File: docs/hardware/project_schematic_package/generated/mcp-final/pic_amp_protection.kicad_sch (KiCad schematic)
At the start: 3 parts, among them U1 MCU, U2 74HC4514, U3 ULN2803A

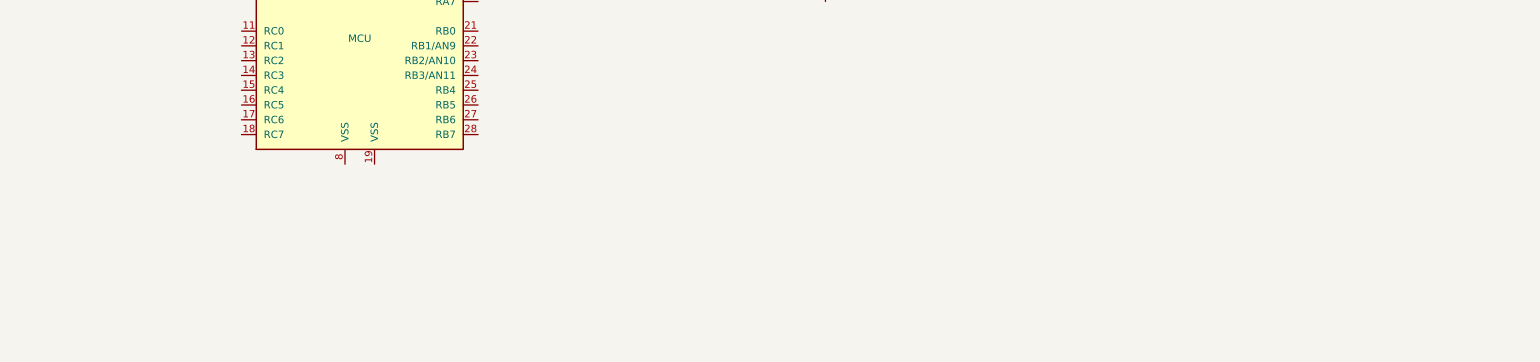
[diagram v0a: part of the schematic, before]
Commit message: Checkpoint MCP schematic layout and developer setup
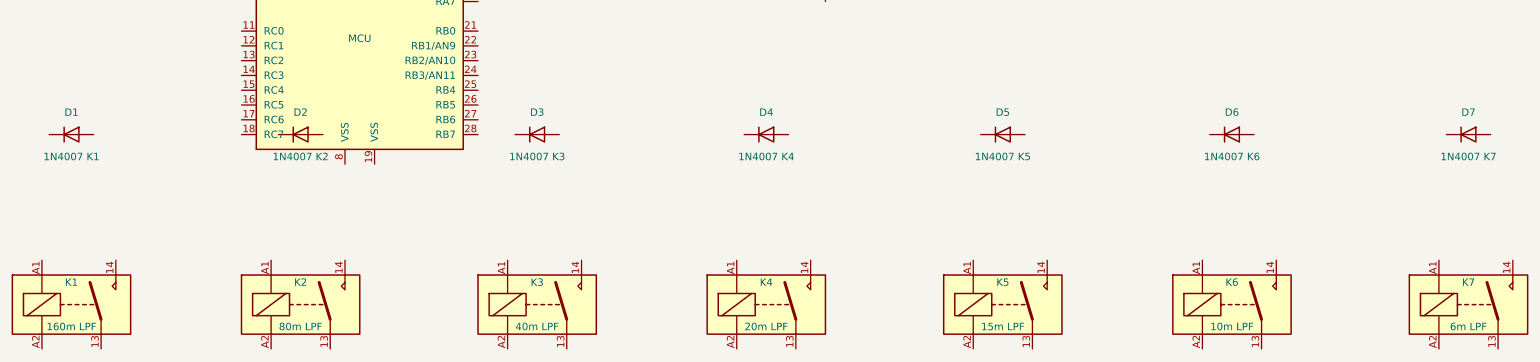
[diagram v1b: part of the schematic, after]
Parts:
- added D1: 1N4007 K1, symbol Device:D
- added D2: 1N4007 K2, symbol Device:D
- added D3: 1N4007 K3, symbol Device:D
- added D4: 1N4007 K4, symbol Device:D
- added D5: 1N4007 K5, symbol Device:D
- added D6: 1N4007 K6, symbol Device:D
- added D7: 1N4007 K7, symbol Device:D
- added K1: 160m LPF, symbol Relay:Relay_SPST-NO
- added K2: 80m LPF, symbol Relay:Relay_SPST-NO
- added K3: 40m LPF, symbol Relay:Relay_SPST-NO
- added K4: 20m LPF, symbol Relay:Relay_SPST-NO
- added K5: 15m LPF, symbol Relay:Relay_SPST-NO
- added K6: 10m LPF, symbol Relay:Relay_SPST-NO
- added K7: 6m LPF, symbol Relay:Relay_SPST-NO

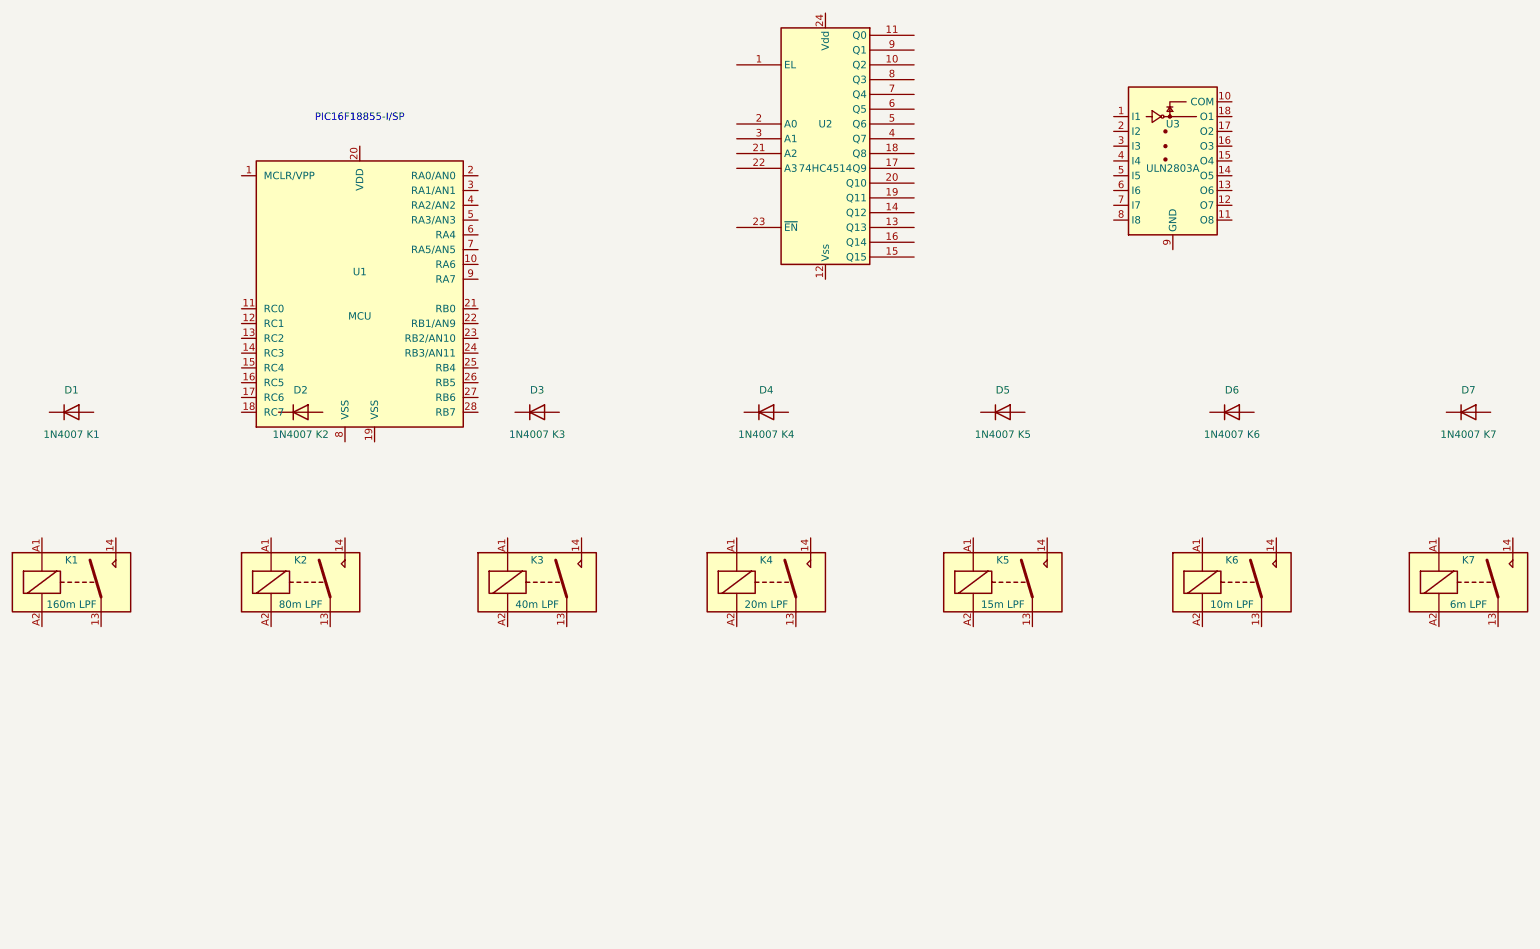
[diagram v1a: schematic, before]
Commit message: Add schematic external interface headers
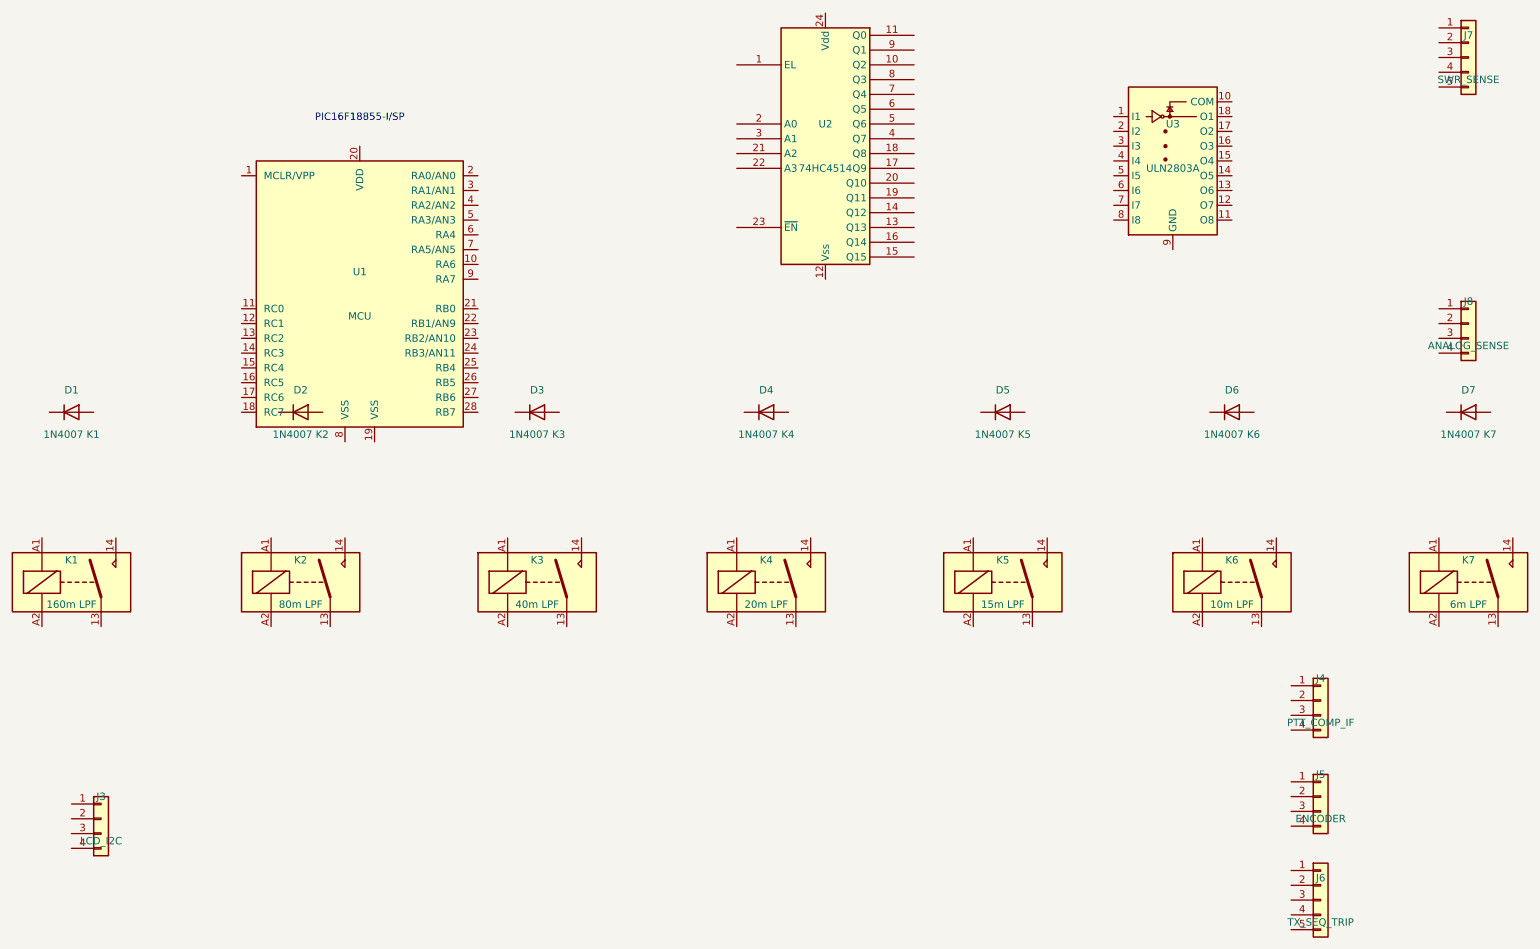
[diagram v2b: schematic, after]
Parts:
- added J3: LCD_I2C, symbol Connector_Generic:Conn_01x04
- added J4: PTT_COMP_IF, symbol Connector_Generic:Conn_01x04
- added J5: ENCODER, symbol Connector_Generic:Conn_01x04
- added J6: TX_SEQ_TRIP, symbol Connector_Generic:Conn_01x05
- added J7: SWR_SENSE, symbol Connector_Generic:Conn_01x05
- added J8: ANALOG_SENSE, symbol Connector_Generic:Conn_01x04

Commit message: Assign PIC16F18855 narrow SPDIP footprint
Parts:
- U1: footprint (none) -> Package_DIP:DIP-28_W7.62mm
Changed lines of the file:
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@@
 		)
 	)
-	(property "Footprint" ""
+	(property "Footprint" "Package_DIP:DIP-28_W7.62mm"
 		(at 80.01 95.25 0)
 		(effects
@@
 			(unit 1)
 			(value "MCU")
-			(footprint "")
+			(footprint "Package_DIP:DIP-28_W7.62mm")
 		)
 		(path "/5f892659-1480-447d-b5a7-bee1c920df64/b79ec903-e143-4f75-9899-3a3ede06d9cd"

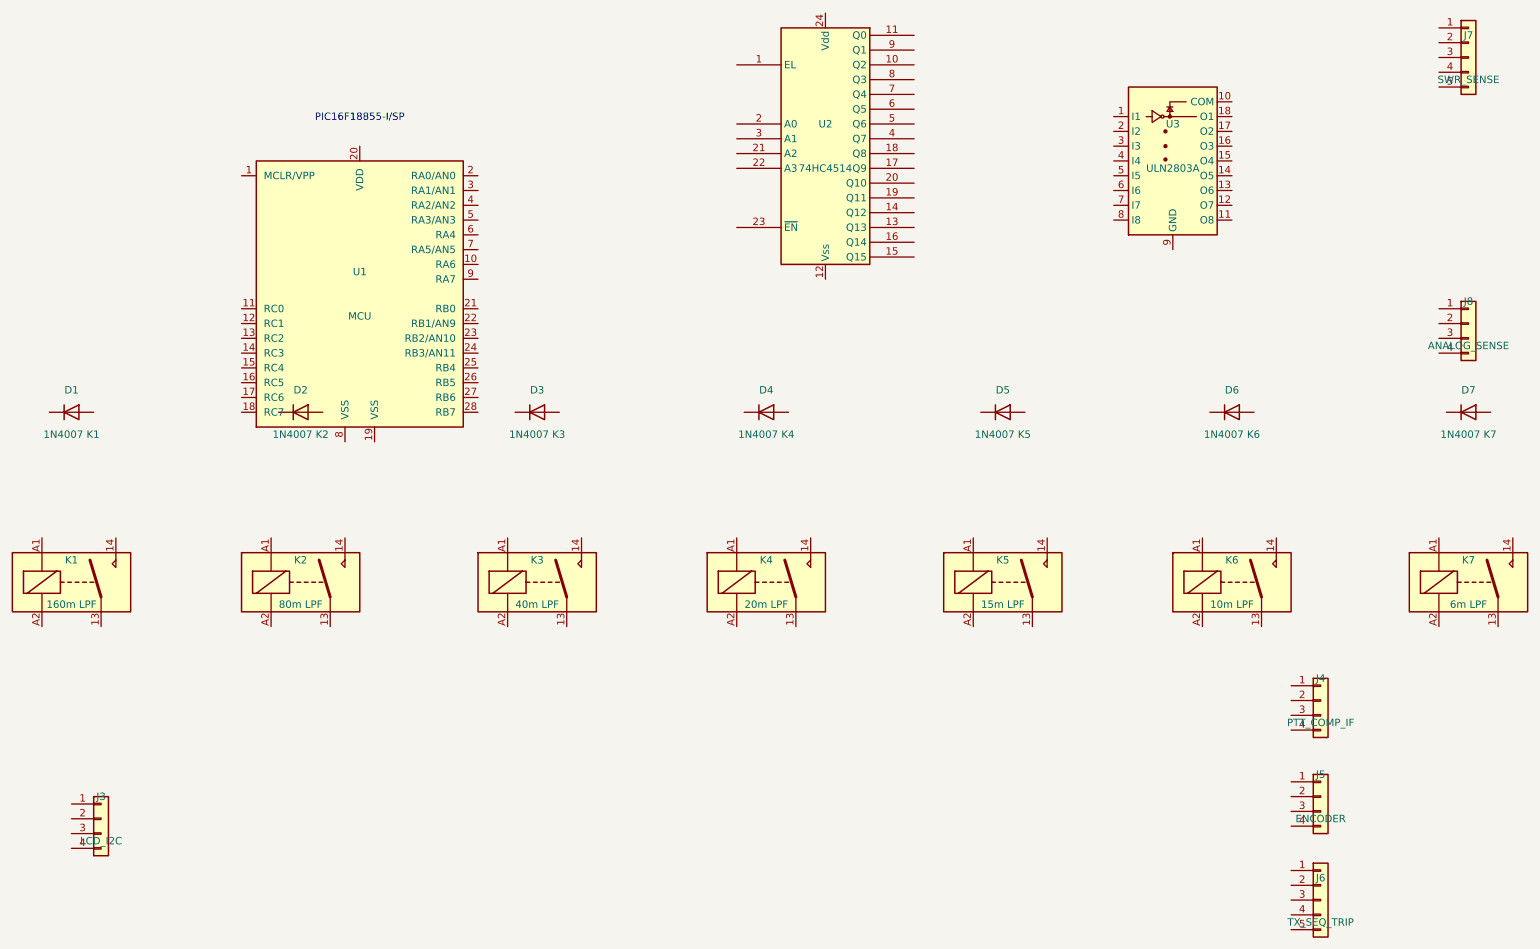
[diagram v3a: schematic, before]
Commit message: Move band decoder and relay driver into child sheet
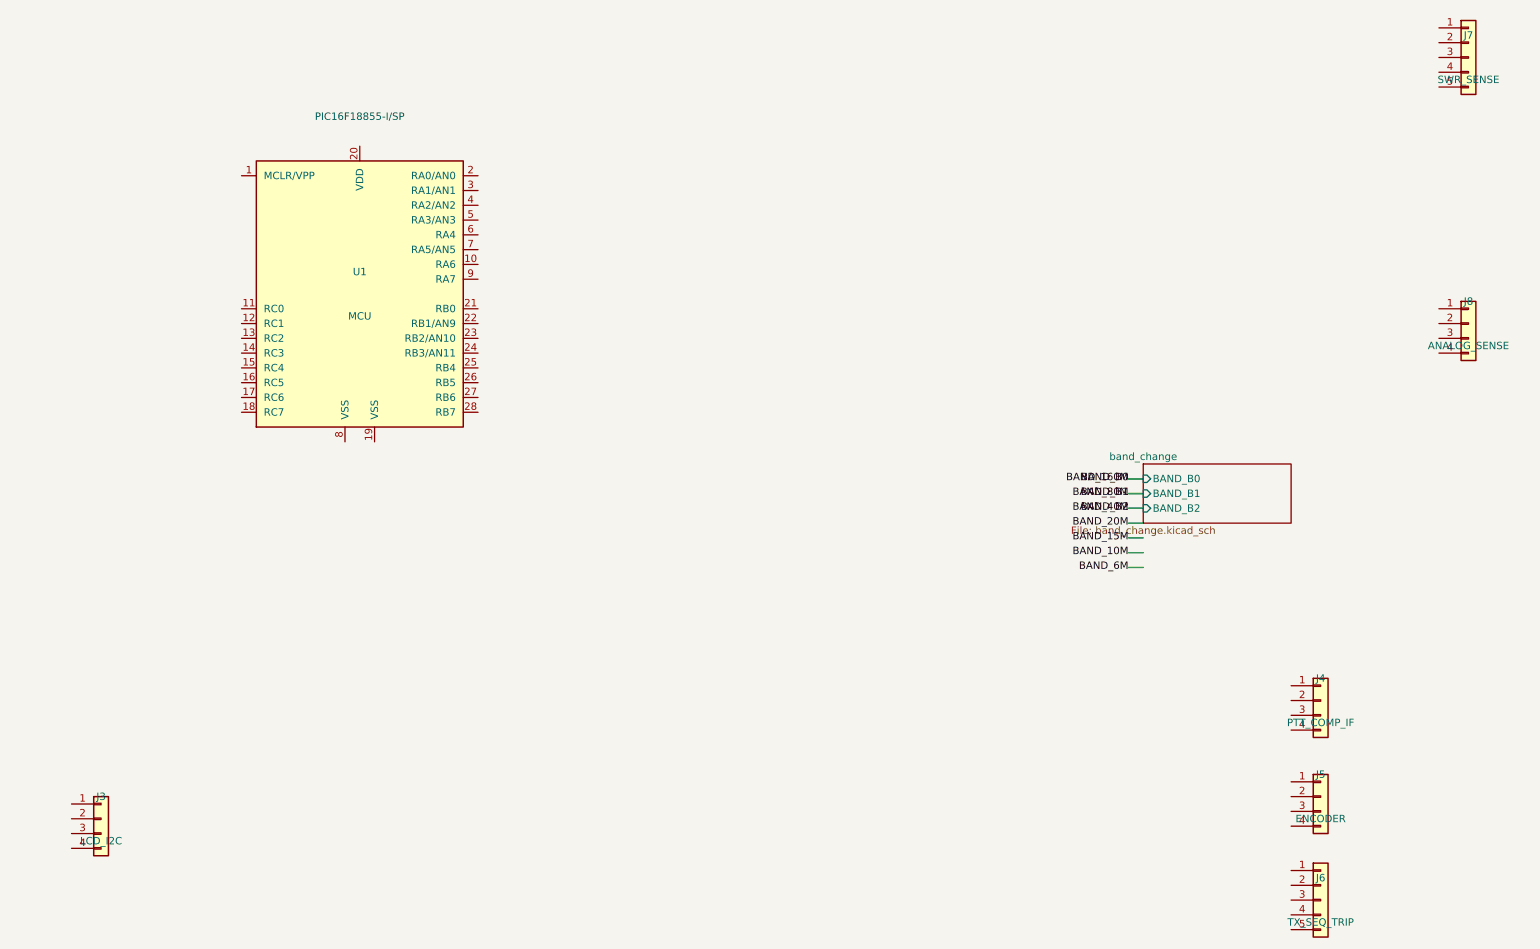
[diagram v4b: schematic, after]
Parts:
- removed D1: 1N4007 K1, symbol Device:D
- removed D2: 1N4007 K2, symbol Device:D
- removed D3: 1N4007 K3, symbol Device:D
- removed D4: 1N4007 K4, symbol Device:D
- removed D5: 1N4007 K5, symbol Device:D
- removed D6: 1N4007 K6, symbol Device:D
- removed D7: 1N4007 K7, symbol Device:D
- removed K1: 160m LPF, symbol Relay:Relay_SPST-NO
- removed K2: 80m LPF, symbol Relay:Relay_SPST-NO
- removed K3: 40m LPF, symbol Relay:Relay_SPST-NO
- removed K4: 20m LPF, symbol Relay:Relay_SPST-NO
- removed K5: 15m LPF, symbol Relay:Relay_SPST-NO
- removed K6: 10m LPF, symbol Relay:Relay_SPST-NO
- removed K7: 6m LPF, symbol Relay:Relay_SPST-NO
- removed U2: 74HC4514, symbol 4xxx_IEEE:4514
- removed U3: ULN2803A, symbol Transistor_Array:ULN2803A
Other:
- added sheet band_change (band_change.kicad_sch)
